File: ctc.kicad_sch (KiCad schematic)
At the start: 11 parts, among them K15 74LS04, U16 Z8430, U17 74LS393, U2 74LS74

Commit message: Upgrade to KiCAD 9.0
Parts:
- renumbered R56 to R19, R56 to R20, R56 to R21, R56 to R22, K15 to UB9, U2 to UC8, U17 to UC9, U16 to UD10, XTAL3 to XTAL2
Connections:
- net at R19.1, UB9.5, XTAL2.2: now also UB9.2; no longer UB9.4
- net at R19.2, R20.2: now also UB9.1; no longer UB9.3
- net at R21.1, R22.2: now also UB9.13; no longer UB9.3
- net at R20.1, R21.2: now also UB9.12; no longer UB9.4

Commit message: Assigned default footprints to ICs
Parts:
- UB9, UC8, UC9: footprint (none) -> Package_DIP:DIP-14_W7.62mm
- UD10: footprint (none) -> Package_DIP:DIP-28_W7.62mm
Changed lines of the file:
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@@
 			)
 		)
-		(property "Footprint" ""
+		(property "Footprint" "Package_DIP:DIP-14_W7.62mm"
 			(at 242.57 68.58 0)
 			(effects
@@
 			)
 		)
-		(property "Footprint" ""
+		(property "Footprint" "Package_DIP:DIP-14_W7.62mm"
 			(at 214.63 66.04 0)
 			(effects
@@
 			)
 		)
-		(property "Footprint" ""
+		(property "Footprint" "Package_DIP:DIP-14_W7.62mm"
 			(at 69.85 118.11 0)
 			(effects
@@
 			)
 		)
-		(property "Footprint" ""
+		(property "Footprint" "Package_DIP:DIP-28_W7.62mm"
 			(at 51.435 30.48 0)
 			(effects
@@
 			)
 		)
-		(property "Footprint" ""
+		(property "Footprint" "Package_DIP:DIP-14_W7.62mm"
 			(at 148.59 66.04 0)
 			(effects
@@
 			)
 		)
-		(property "Footprint" ""
+		(property "Footprint" "Package_DIP:DIP-14_W7.62mm"
 			(at 181.61 66.04 0)
 			(effects
@@
 			)
 		)
-		(property "Footprint" ""
+		(property "Footprint" "Package_DIP:DIP-14_W7.62mm"
 			(at 190.5 116.84 0)
 			(effects

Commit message: Fixed packages
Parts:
- UD10: footprint Package_DIP:DIP-28_W7.62mm -> Package_DIP:DIP-28_W15.24mm
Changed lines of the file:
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@@
 			)
 		)
-		(property "Footprint" "Package_DIP:DIP-28_W7.62mm"
+		(property "Footprint" "Package_DIP:DIP-28_W15.24mm"
 			(at 51.435 30.48 0)
 			(effects

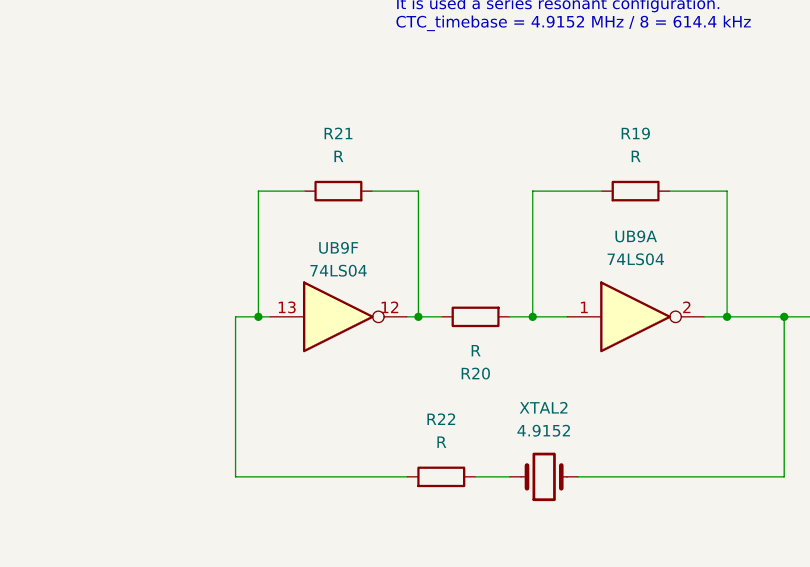
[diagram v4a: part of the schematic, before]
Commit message: pcb: added and placed almost all components
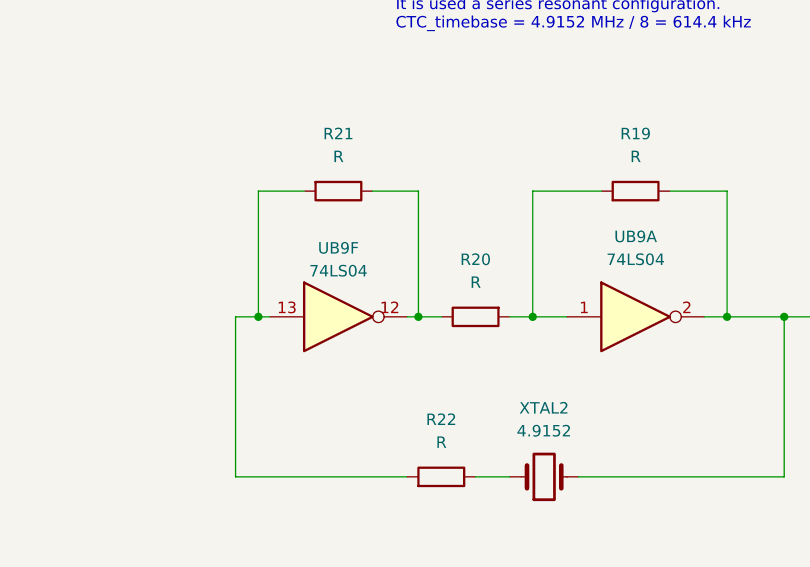
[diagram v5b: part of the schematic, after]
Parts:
- R19, R20, R21, R22, R9: footprint (none) -> Resistor_THT:R_Axial_DIN0204_L3.6mm_D1.6mm_P5.08mm_Vertical
- XTAL2: footprint (none) -> Crystal:Crystal_HC18-U_Vertical
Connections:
- net at R22.2, UB9.13: now also R21.2; no longer R21.1
- net at R20.1, UB9.12: now also R21.1; no longer R21.2
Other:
- moved on the sheet: R21
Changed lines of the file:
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@@
 			)
 		)
-		(property "Footprint" ""
+		(property "Footprint" "Crystal:Crystal_HC18-U_Vertical"
 			(at 171.45 83.82 0)
 			(effects
@@
 			)
 		)
-		(property "Footprint" ""
+		(property "Footprint" "Resistor_THT:R_Axial_DIN0204_L3.6mm_D1.6mm_P5.08mm_Vertical"
 			(at 181.61 53.848 90)
 			(effects
@@
 	(symbol
 		(lib_id "Device:R")
-		(at 148.59 52.07 90)
+		(at 148.59 52.07 270)
 		(unit 1)
 		(exclude_from_sim no)
@@
 			)
 		)
-		(property "Footprint" ""
-			(at 148.59 53.848 90)
+		(property "Footprint" "Resistor_THT:R_Axial_DIN0204_L3.6mm_D1.6mm_P5.08mm_Vertical"
+			(at 148.59 50.292 90)
 			(effects
 				(font
@@
 			)
 		)
-		(property "Footprint" ""
+		(property "Footprint" "Resistor_THT:R_Axial_DIN0204_L3.6mm_D1.6mm_P5.08mm_Vertical"
 			(at 24.892 66.04 90)
 			(effects
@@
 			)
 		)
-		(property "Footprint" ""
+		(property "Footprint" "Resistor_THT:R_Axial_DIN0204_L3.6mm_D1.6mm_P5.08mm_Vertical"
 			(at 160.02 85.598 90)
 			(effects
@@
 		(fields_autoplaced yes)
 		(property "Reference" "R20"
-			(at 163.83 72.39 90)
+			(at 163.83 59.69 90)
 			(effects
 				(font
@@
 		)
 		(property "Value" "R"
-			(at 163.83 69.85 90)
-			(effects
-				(font
-					(size 1.27 1.27)
-				)
-			)
-		)
-		(property "Footprint" ""
+			(at 163.83 62.23 90)
+			(effects
+				(font
+					(size 1.27 1.27)
+				)
+			)
+		)
+		(property "Footprint" "Resistor_THT:R_Axial_DIN0204_L3.6mm_D1.6mm_P5.08mm_Vertical"
 			(at 163.83 64.262 90)
 			(effects

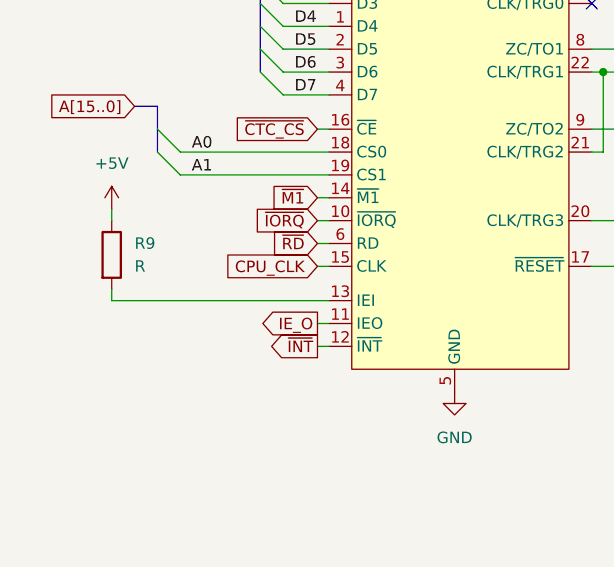
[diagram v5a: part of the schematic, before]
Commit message: pcb: added all the connector, 99% routed
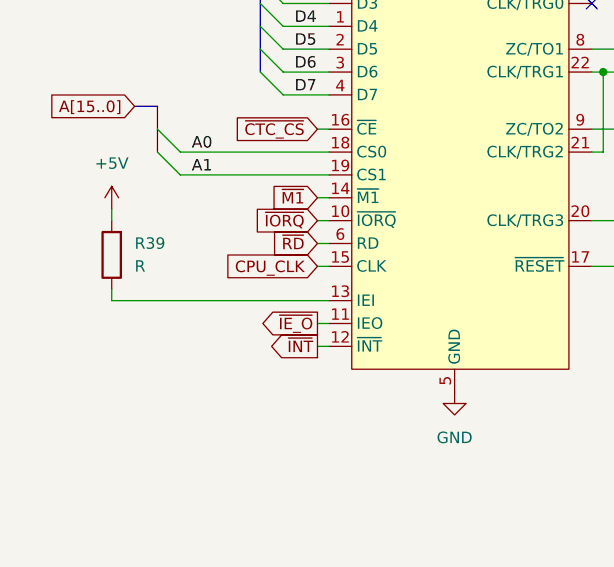
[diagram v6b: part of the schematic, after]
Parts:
- renumbered R9 to R39
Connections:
- net +5V: now also R39.2; no longer R39.1
- net at UD10.13 (IEI): now also R39.1; no longer R39.2
- net IE_O renamed ~{IE_O}
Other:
- moved on the sheet: R39
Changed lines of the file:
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@@
 		)
 	)
-	(global_label "IE_O"
+	(global_label "~{IE_O}"
 		(shape output)
 		(at 49.53 73.66 180)
@@
 	(symbol
 		(lib_id "Device:R")
-		(at 26.67 66.04 0)
+		(at 26.67 66.04 180)
 		(unit 1)
 		(exclude_from_sim no)
@@
 		(dnp no)
 		(fields_autoplaced yes)
-		(property "Reference" "R9"
-			(at 29.21 64.77 0)
-			(effects
-				(font
-					(size 1.27 1.27)
-				)
-				(justify left)
+		(property "Reference" "R39"
+			(at 29.21 64.7699 0)
+			(effects
+				(font
+					(size 1.27 1.27)
+				)
+				(justify right)
 			)
 		)
 		(property "Value" "R"
-			(at 29.21 67.31 0)
-			(effects
-				(font
-					(size 1.27 1.27)
-				)
-				(justify left)
+			(at 29.21 67.3099 0)
+			(effects
+				(font
+					(size 1.27 1.27)
+				)
+				(justify right)
 			)
 		)
 		(property "Footprint" "Resistor_THT:R_Axial_DIN0204_L3.6mm_D1.6mm_P5.08mm_Vertical"
-			(at 24.892 66.04 90)
+			(at 28.448 66.04 90)
 			(effects
 				(font
@@
 			(project "ceda"
 				(path "/12a6dbe3-008d-4c5b-88f6-9f1c816060be/08d69802-ecbf-4783-8ee3-1052eb874de4"
-					(reference "R9")
+					(reference "R39")
 					(unit 1)
 				)
